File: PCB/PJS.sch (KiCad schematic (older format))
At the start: 40 parts, among them J1 HFW8R-1STE1H1LF_FFC, J10 SM02B-PASS-TBT_SwitchConnector, J2 SM02B-PASS-TBT_Connector, J3 SM02B-PASS-TBT_Connector, J4 SM02B-PASS-TBT_Connector, J5 SM02B-PASS-TBT_Connector, J6 SM02B-PASS-TBT_SwitchConnector, J7 SM02B-PASS-TBT_SwitchConnector, J8 SM02B-PASS-TBT_SwitchConnector, J9 SM02B-PASS-TBT_SwitchConnector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

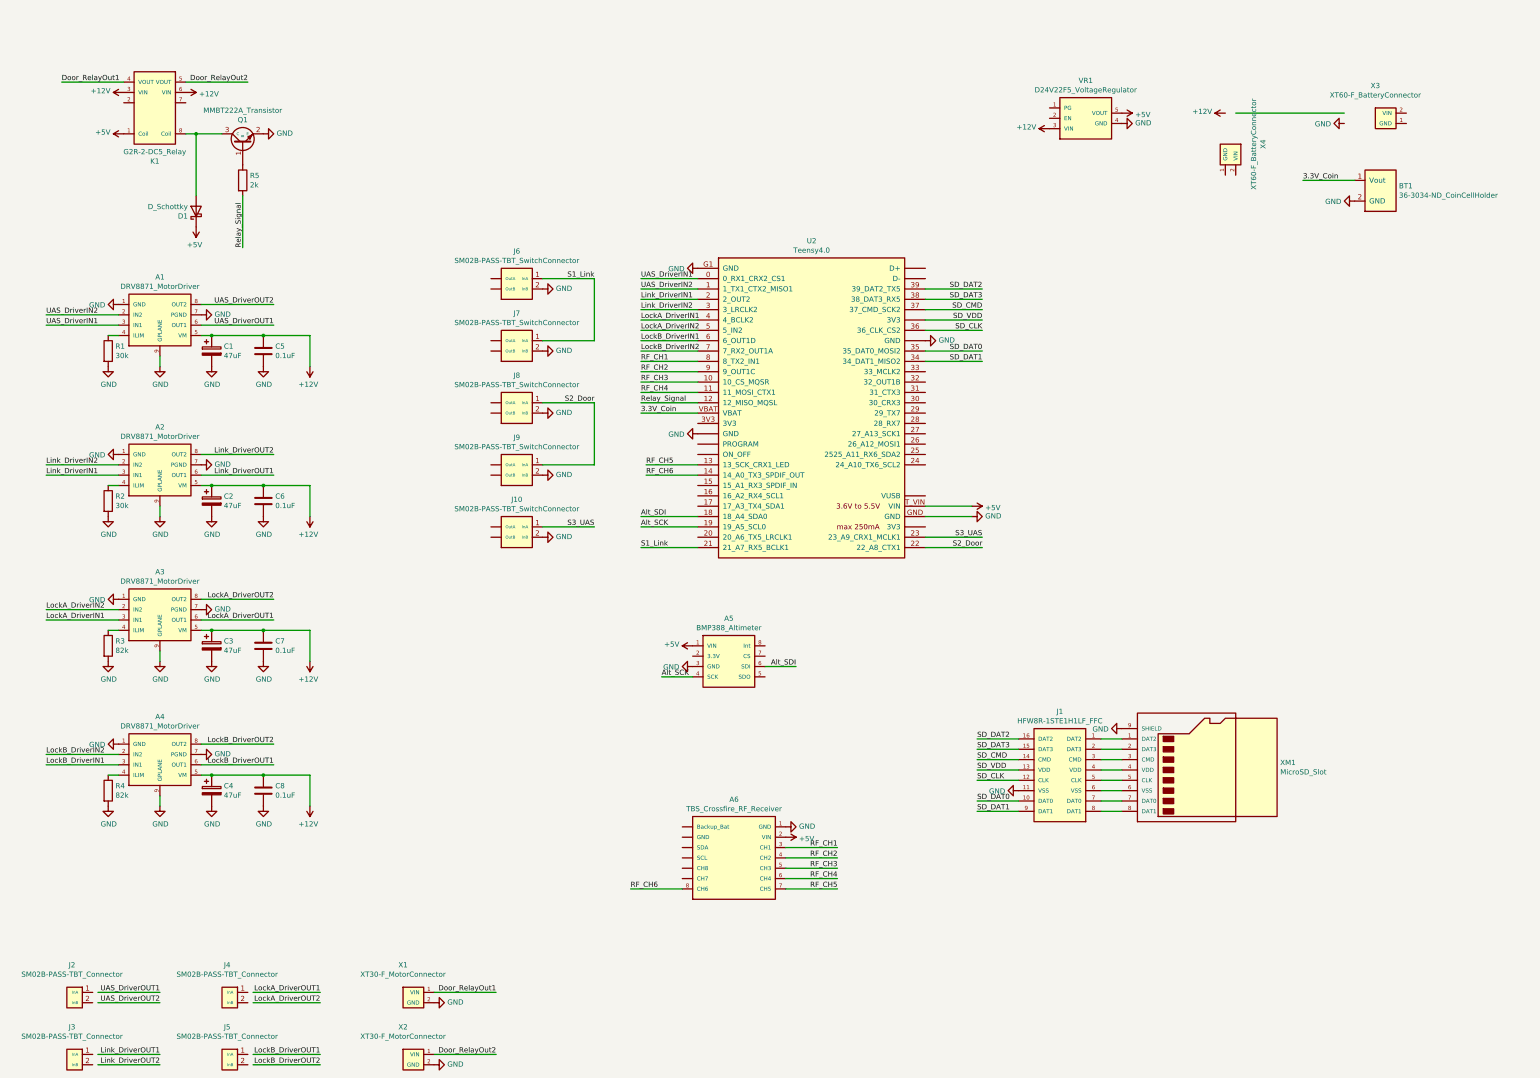
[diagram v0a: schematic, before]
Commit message: Updated connector symbols
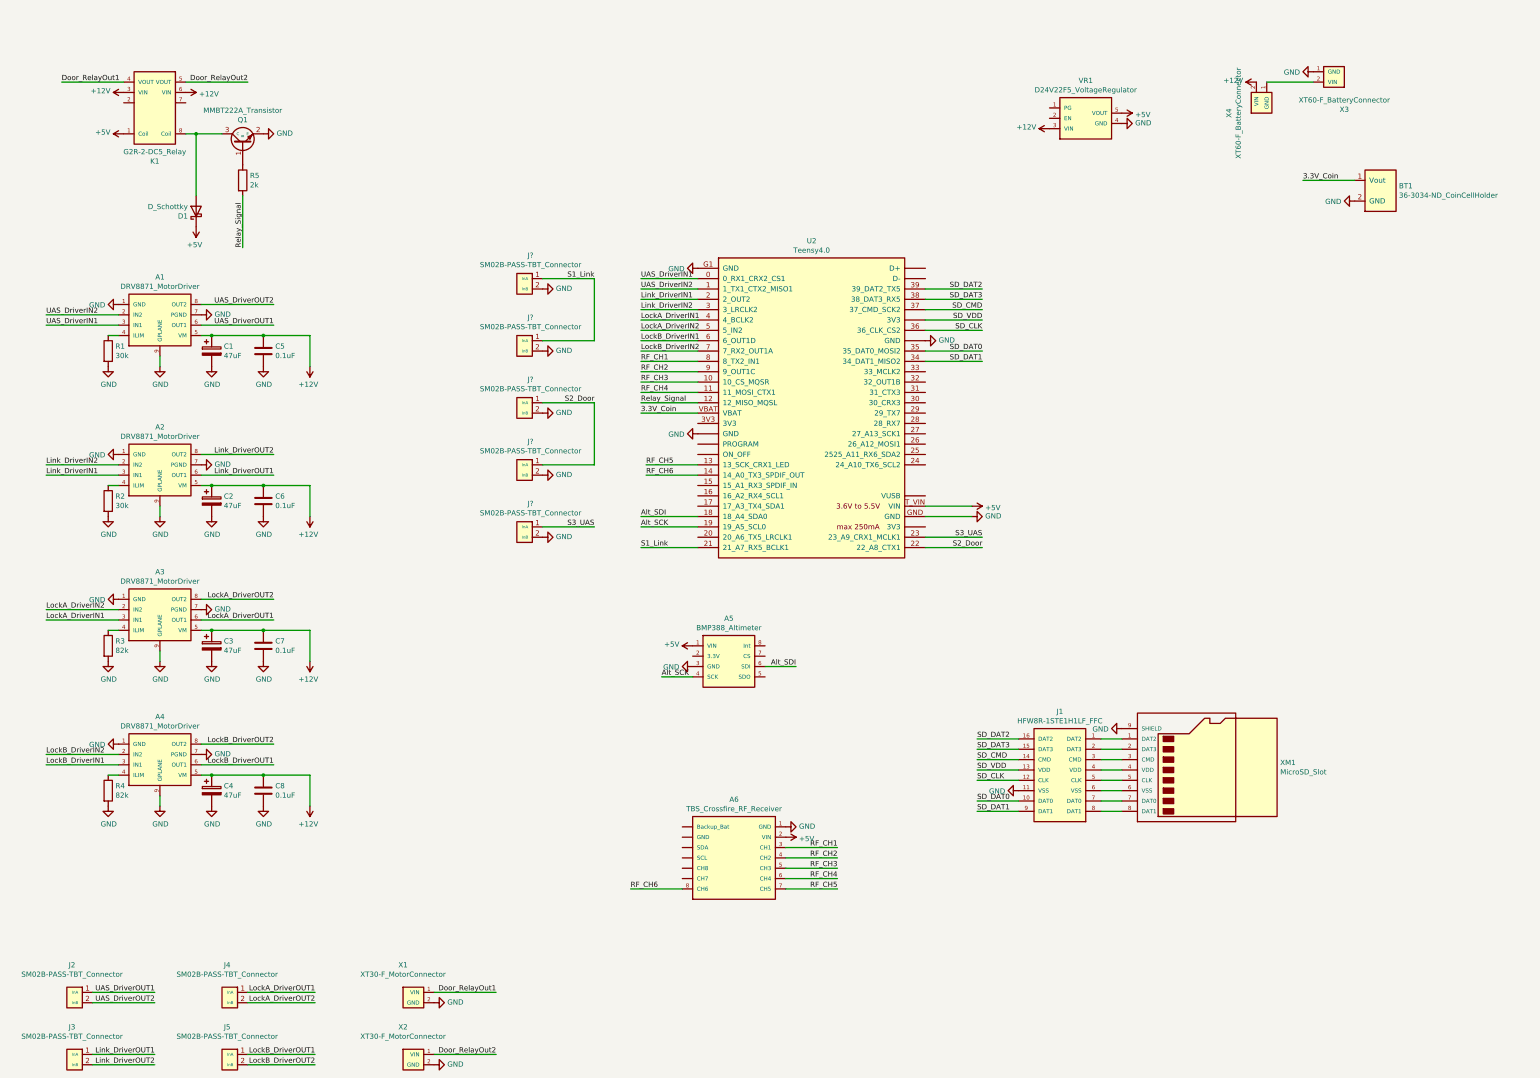
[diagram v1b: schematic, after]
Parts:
- removed J10, J6, J7, J8, J9: SM02B-PASS-TBT_SwitchConnector, PJS:SM02B-PASS-TBT_Connector, symbol PJS:SM02B-PASS-TBT_SwitchConnector
- added J? (x5): SM02B-PASS-TBT_Connector, symbol PJS:SM02B-PASS-TBT_Connector
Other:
- moved on the sheet: X3, X4
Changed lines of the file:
@@
 Wire Wire Line
 	8300 8850 8800 8850
-Text Label 2250 10150 2    50   ~ 0
+Text Label 2200 10150 2    50   ~ 0
 UAS_DriverOUT1
-Text Label 2250 10250 2    50   ~ 0
+Text Label 2200 10250 2    50   ~ 0
 UAS_DriverOUT2
 Text Label 6900 3250 0    50   ~ 0
@@
 Text Label 6900 3350 0    50   ~ 0
 UAS_DriverIN2
-Text Label 2250 10750 2    50   ~ 0
+Text Label 2200 10750 2    50   ~ 0
 Link_DriverOUT1
-Text Label 2250 10850 2    50   ~ 0
+Text Label 2200 10850 2    50   ~ 0
 Link_DriverOUT2
 $Comp
@@
 $EndComp
 Wire Wire Line
-	1650 10150 2250 10150
-Wire Wire Line
-	1650 10250 2250 10250
-Wire Wire Line
-	1650 10750 2250 10750
-Wire Wire Line
-	1650 10850 2250 10850
+	1600 10150 2200 10150
+Wire Wire Line
+	1600 10250 2200 10250
+Wire Wire Line
+	1600 10750 2200 10750
+Wire Wire Line
+	1600 10850 2200 10850
 Wire Wire Line
 	6900 5650 7450 5650
@@
 	0    -1   -1   0
 $EndComp
-Text Label 3800 10150 2    50   ~ 0
+Text Label 3750 10150 2    50   ~ 0
 LockA_DriverOUT1
-Text Label 3800 10250 2    50   ~ 0
+Text Label 3750 10250 2    50   ~ 0
 LockA_DriverOUT2
-Text Label 3800 10750 2    50   ~ 0
+Text Label 3750 10750 2    50   ~ 0
 LockB_DriverOUT1
-Text Label 3800 10850 2    50   ~ 0
+Text Label 3750 10850 2    50   ~ 0
 LockB_DriverOUT2
 Text Label 6450 4450 2    50   ~ 0
@@
 L power:GND #PWR0134
 U 1 1 5FF2647A
-P 13700 1750
-F 0 "#PWR0134" H 13700 1500 50  0001 C CNN
-F 1 "GND" V 13705 1622 50  0000 R CNN
-F 2 "" H 13700 1750 50  0001 C CNN
-F 3 "" H 13700 1750 50  0001 C CNN
-	1    13700 1750
+P 13400 1250
+F 0 "#PWR0134" H 13400 1000 50  0001 C CNN
+F 1 "GND" V 13405 1122 50  0000 R CNN
+F 2 "" H 13400 1250 50  0001 C CNN
+F 3 "" H 13400 1250 50  0001 C CNN
+	1    13400 1250
 	0    1    1    0
 $EndComp
@@
 L PJS:XT60-F_BatteryConnector X3
 U 1 1 5FF22EAF
-P 14000 1700
-F 0 "X3" H 14000 2015 50  0000 C CNN
-F 1 "XT60-F_BatteryConnector" H 14000 1924 50  0000 C CNN
-F 2 "PJS:XT60_FemaleBatteryConnector" H 14000 2200 50  0001 C CNN
-F 3 "" H 14000 2200 50  0001 C CNN
-	1    14000 1700
-	1    0    0    -1
+P 13700 1300
+F 0 "X3" H 13700 1615 50  0000 C CNN
+F 1 "XT60-F_BatteryConnector" H 13700 1524 50  0000 C CNN
+F 2 "PJS:XT60_FemaleBatteryConnector" H 13700 1800 50  0001 C CNN
+F 3 "" H 13700 1800 50  0001 C CNN
+	1    13700 1300
+	-1   0    0    1
 $EndComp
 $Comp
@@
 	2650 6650 2750 6650
 Wire Wire Line
-	3150 10850 3800 10850
-Wire Wire Line
-	3150 10750 3800 10750
-Wire Wire Line
-	3150 10250 3800 10250
-Wire Wire Line
-	3150 10150 3800 10150
+	3100 10850 3750 10850
+Wire Wire Line
+	3100 10750 3750 10750
+Wire Wire Line
+	3100 10250 3750 10250
+Wire Wire Line
+	3100 10150 3750 10150
 $Comp
 L power:GND #PWR0153
@@
 L PJS:XT60-F_BatteryConnector X4
 U 1 1 5FF20F6C
-P 12600 1950
-F 0 "X4" H 12600 2265 50  0000 C CNN
-F 1 "XT60-F_BatteryConnector" H 12600 2174 50  0000 C CNN
-F 2 "PJS:XT60_FemaleBatteryConnector" H 12600 2450 50  0001 C CNN
-F 3 "" H 12600 2450 50  0001 C CNN
-	1    12600 1950
-	0    1    1    0
-$EndComp
-Wire Wire Line
-	13700 1650 12650 1650
+P 12900 1650
+F 0 "X4" H 12900 1965 50  0000 C CNN
+F 1 "XT60-F_BatteryConnector" H 12900 1874 50  0000 C CNN
+F 2 "PJS:XT60_FemaleBatteryConnector" H 12900 2150 50  0001 C CNN
+F 3 "" H 12900 2150 50  0001 C CNN
+	1    12900 1650
+	0    -1   -1   0
+$EndComp
 $Comp
 L power:+12V #PWR0135
 U 1 1 5FF3DFBC
-P 12550 1650
-F 0 "#PWR0135" H 12550 1500 50  0001 C CNN
-F 1 "+12V" V 12565 1778 50  0000 L CNN
-F 2 "" H 12550 1650 50  0001 C CNN
-F 3 "" H 12550 1650 50  0001 C CNN
-	1    12550 1650
-	0    -1   -1   0
-$EndComp
-$Comp
-L PJS:SM02B-PASS-TBT_SwitchConnector J7
-U 1 1 5FF5A567
-P 5700 3900
-F 0 "J7" H 5700 4215 50  0000 C CNN
-F 1 "SM02B-PASS-TBT_SwitchConnector" H 5700 4124 50  0000 C CNN
-F 2 "PJS:SM02B-PASS-TBT_Connector" H 5700 4700 50  0001 C CNN
-F 3 "" H 5700 4700 50  0001 C CNN
-	1    5700 3900
-	1    0    0    -1
-$EndComp
-$Comp
-L PJS:SM02B-PASS-TBT_SwitchConnector J8
-U 1 1 5FF60366
-P 5700 4500
-F 0 "J8" H 5700 4815 50  0000 C CNN
-F 1 "SM02B-PASS-TBT_SwitchConnector" H 5700 4724 50  0000 C CNN
-F 2 "PJS:SM02B-PASS-TBT_Connector" H 5700 5300 50  0001 C CNN
-F 3 "" H 5700 5300 50  0001 C CNN
-	1    5700 4500
-	1    0    0    -1
+P 12850 1350
+F 0 "#PWR0135" H 12850 1200 50  0001 C CNN
+F 1 "+12V" V 12865 1478 50  0000 L CNN
+F 2 "" H 12850 1350 50  0001 C CNN
+F 3 "" H 12850 1350 50  0001 C CNN
+	1    12850 1350
+	0    -1   -1   0
 $EndComp
 $Comp
@@
 Text Label 6450 5650 2    50   ~ 0
 S3_UAS
-$Comp
-L PJS:SM02B-PASS-TBT_SwitchConnector J6
-U 1 1 5FF52CF4
-P 5700 3300
-F 0 "J6" H 5700 3615 50  0000 C CNN
-F 1 "SM02B-PASS-TBT_SwitchConnector" H 5700 3524 50  0000 C CNN
-F 2 "PJS:SM02B-PASS-TBT_Connector" H 5700 4100 50  0001 C CNN
-F 3 "" H 5700 4100 50  0001 C CNN
-	1    5700 3300
-	1    0    0    -1
-$EndComp
-$Comp
-L PJS:SM02B-PASS-TBT_SwitchConnector J9
-U 1 1 5FF66278
-P 5700 5100
-F 0 "J9" H 5700 5415 50  0000 C CNN
-F 1 "SM02B-PASS-TBT_SwitchConnector" H 5700 5324 50  0000 C CNN
-F 2 "PJS:SM02B-PASS-TBT_Connector" H 5700 5900 50  0001 C CNN
-F 3 "" H 5700 5900 50  0001 C CNN
-	1    5700 5100
-	1    0    0    -1
-$EndComp
-$Comp
-L PJS:SM02B-PASS-TBT_SwitchConnector J10
-U 1 1 5FF6C1E4
-P 5700 5700
-F 0 "J10" H 5700 6015 50  0000 C CNN
-F 1 "SM02B-PASS-TBT_SwitchConnector" H 5700 5924 50  0000 C CNN
-F 2 "PJS:SM02B-PASS-TBT_Connector" H 5700 6500 50  0001 C CNN
-F 3 "" H 5700 6500 50  0001 C CNN
-	1    5700 5700
-	1    0    0    -1
-$EndComp
 Wire Wire Line
 	5950 5650 6450 5650
@@
 	0    1    1    0
 $EndComp
+$Comp
+L PJS:SM02B-PASS-TBT_Connector J?
+U 1 1 5FF34C1C
+P 5750 3300
+F 0 "J?" H 5833 3575 50  0000 C CNN
+F 1 "SM02B-PASS-TBT_Connector" H 5833 3484 50  0000 C CNN
+F 2 "" H 5750 4100 50  0001 C CNN
+F 3 "" H 5750 4100 50  0001 C CNN
+	1    5750 3300
+	1    0    0    -1
+$EndComp
+$Comp
+L PJS:SM02B-PASS-TBT_Connector J?
+U 1 1 5FF35CEB
+P 5750 3900
+F 0 "J?" H 5833 4175 50  0000 C CNN
+F 1 "SM02B-PASS-TBT_Connector" H 5833 4084 50  0000 C CNN
+F 2 "" H 5750 4700 50  0001 C CNN
+F 3 "" H 5750 4700 50  0001 C CNN
+	1    5750 3900
+	1    0    0    -1
+$EndComp
+$Comp
+L PJS:SM02B-PASS-TBT_Connector J?
+U 1 1 5FF3C0BA
+P 5750 4500
+F 0 "J?" H 5833 4775 50  0000 C CNN
+F 1 "SM02B-PASS-TBT_Connector" H 5833 4684 50  0000 C CNN
+F 2 "" H 5750 5300 50  0001 C CNN
+F 3 "" H 5750 5300 50  0001 C CNN
+	1    5750 4500
+	1    0    0    -1
+$EndComp
+$Comp
+L PJS:SM02B-PASS-TBT_Connector J?
+U 1 1 5FF423A5
+P 5750 5100
+F 0 "J?" H 5833 5375 50  0000 C CNN
+F 1 "SM02B-PASS-TBT_Connector" H 5833 5284 50  0000 C CNN
+F 2 "" H 5750 5900 50  0001 C CNN
+F 3 "" H 5750 5900 50  0001 C CNN
+	1    5750 5100
+	1    0    0    -1
+$EndComp
+$Comp
+L PJS:SM02B-PASS-TBT_Connector J?
+U 1 1 5FF486F6
+P 5750 5700
+F 0 "J?" H 5833 5975 50  0000 C CNN
+F 1 "SM02B-PASS-TBT_Connector" H 5833 5884 50  0000 C CNN
+F 2 "" H 5750 6500 50  0001 C CNN
+F 3 "" H 5750 6500 50  0001 C CNN
+	1    5750 5700
+	1    0    0    -1
+$EndComp
+Wire Wire Line
+	13400 1350 12950 1350
 $EndSCHEMATC

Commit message: Nearly Finished PCB
Requires resizing footprint for the altimeter. New resistors on the motor driver ICs need to be implemented. Perhaps ground planes/heat dissapation should be added to the driver ICs.
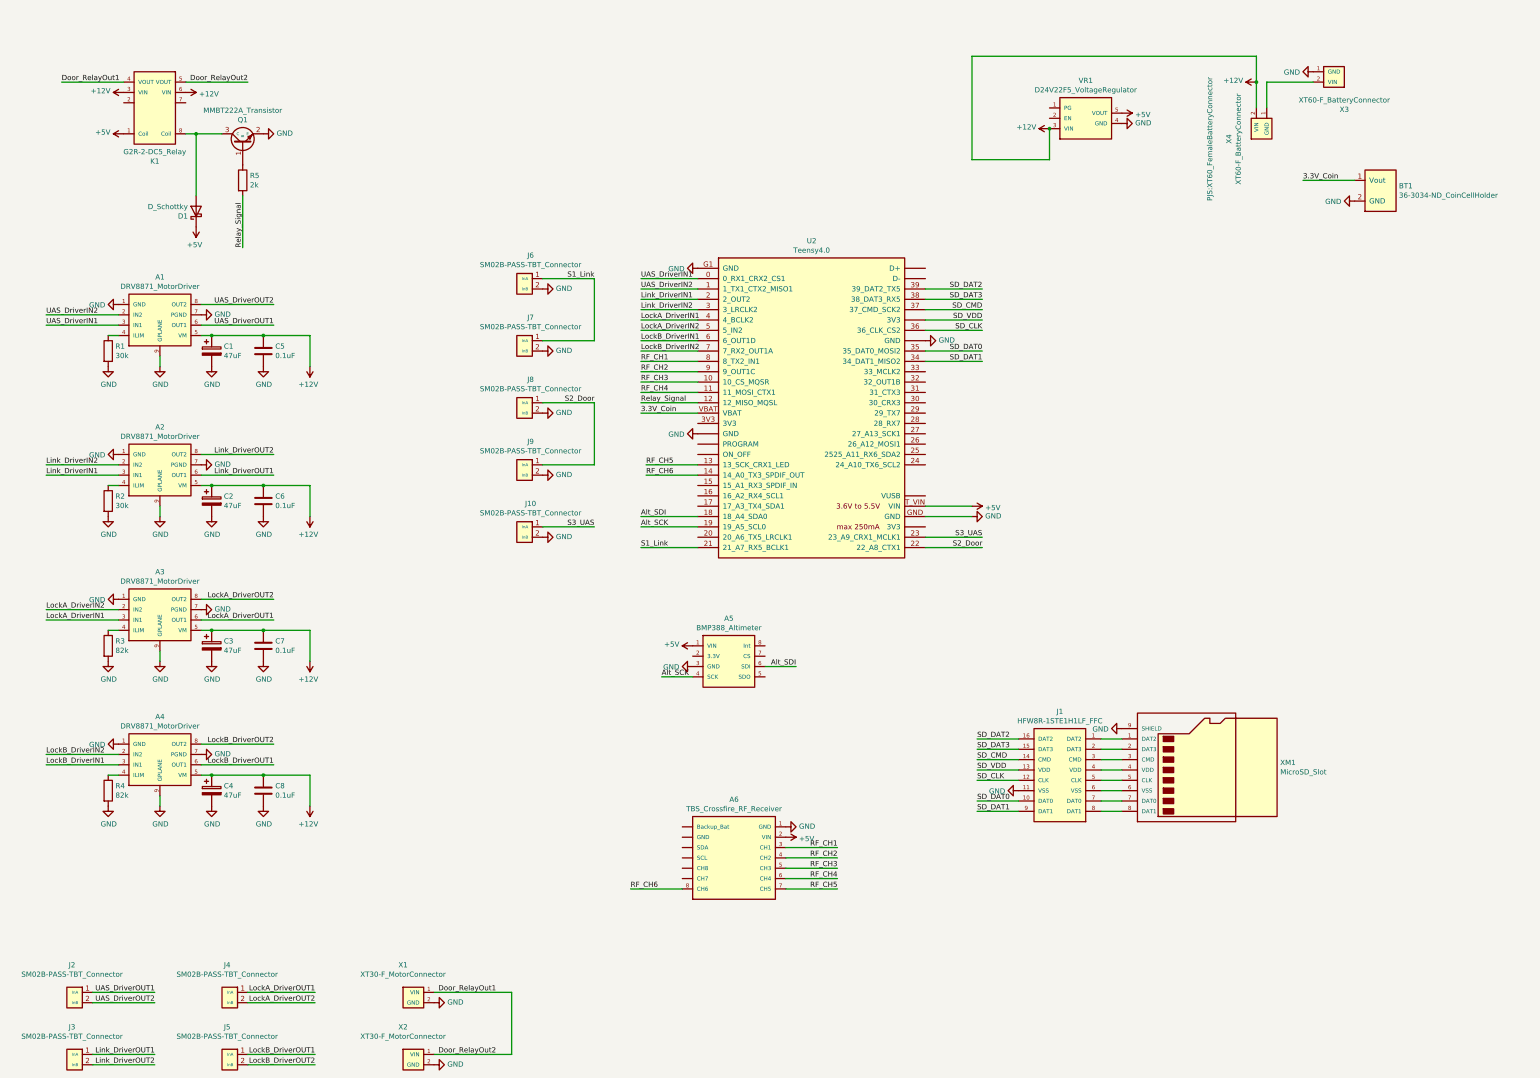
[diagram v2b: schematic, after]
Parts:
- gave numbers to parts that had none: 5
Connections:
- net Door_RelayOut2 is gone; now on net Door_RelayOut1: K1.5 (VOUT), X2.1 (VIN)
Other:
- moved on the sheet: X4
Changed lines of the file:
@@
 	0    -1   -1   0
 $EndComp
-Wire Wire Line
-	4900 10750 5500 10750
 $Comp
 L PJS:XT30-F_MotorConnector X2
@@
 	1    0    0    -1
 $EndComp
-Wire Wire Line
-	4900 10150 5500 10150
 Text Label 5500 10750 2    50   ~ 0
 Door_RelayOut2
@@
 L PJS:XT60-F_BatteryConnector X4
 U 1 1 5FF20F6C
-P 12900 1650
-F 0 "X4" H 12900 1965 50  0000 C CNN
-F 1 "XT60-F_BatteryConnector" H 12900 1874 50  0000 C CNN
-F 2 "PJS:XT60_FemaleBatteryConnector" H 12900 2150 50  0001 C CNN
-F 3 "" H 12900 2150 50  0001 C CNN
-	1    12900 1650
+P 12900 1900
+F 0 "X4" H 12900 2215 50  0000 C CNN
+F 1 "XT60-F_BatteryConnector" H 12900 2124 50  0000 C CNN
+F 2 "PJS:XT60_FemaleBatteryConnector" H 12900 2400 50  0000 C CNN
+F 3 "" H 12900 2400 50  0001 C CNN
+	1    12900 1900
 	0    -1   -1   0
 $EndComp
@@
 $EndComp
 $Comp
-L PJS:SM02B-PASS-TBT_Connector J?
+L PJS:SM02B-PASS-TBT_Connector J6
 U 1 1 5FF34C1C
 P 5750 3300
-F 0 "J?" H 5833 3575 50  0000 C CNN
+F 0 "J6" H 5833 3575 50  0000 C CNN
 F 1 "SM02B-PASS-TBT_Connector" H 5833 3484 50  0000 C CNN
 F 2 "" H 5750 4100 50  0001 C CNN
@@
 $EndComp
 $Comp
-L PJS:SM02B-PASS-TBT_Connector J?
+L PJS:SM02B-PASS-TBT_Connector J7
 U 1 1 5FF35CEB
 P 5750 3900
-F 0 "J?" H 5833 4175 50  0000 C CNN
+F 0 "J7" H 5833 4175 50  0000 C CNN
 F 1 "SM02B-PASS-TBT_Connector" H 5833 4084 50  0000 C CNN
 F 2 "" H 5750 4700 50  0001 C CNN
@@
 $EndComp
 $Comp
-L PJS:SM02B-PASS-TBT_Connector J?
+L PJS:SM02B-PASS-TBT_Connector J8
 U 1 1 5FF3C0BA
 P 5750 4500
-F 0 "J?" H 5833 4775 50  0000 C CNN
+F 0 "J8" H 5833 4775 50  0000 C CNN
 F 1 "SM02B-PASS-TBT_Connector" H 5833 4684 50  0000 C CNN
 F 2 "" H 5750 5300 50  0001 C CNN
@@
 $EndComp
 $Comp
-L PJS:SM02B-PASS-TBT_Connector J?
+L PJS:SM02B-PASS-TBT_Connector J9
 U 1 1 5FF423A5
 P 5750 5100
-F 0 "J?" H 5833 5375 50  0000 C CNN
+F 0 "J9" H 5833 5375 50  0000 C CNN
 F 1 "SM02B-PASS-TBT_Connector" H 5833 5284 50  0000 C CNN
 F 2 "" H 5750 5900 50  0001 C CNN
@@
 $EndComp
 $Comp
-L PJS:SM02B-PASS-TBT_Connector J?
+L PJS:SM02B-PASS-TBT_Connector J10
 U 1 1 5FF486F6
 P 5750 5700
-F 0 "J?" H 5833 5975 50  0000 C CNN
+F 0 "J10" H 5833 5975 50  0000 C CNN
 F 1 "SM02B-PASS-TBT_Connector" H 5833 5884 50  0000 C CNN
 F 2 "" H 5750 6500 50  0001 C CNN
@@
 Wire Wire Line
 	13400 1350 12950 1350
+Wire Wire Line
+	5650 10150 5650 10750
+Wire Wire Line
+	4900 10750 5650 10750
+Wire Wire Line
+	4900 10150 5650 10150
+Wire Wire Line
+	12950 1600 12950 1350
+Wire Wire Line
+	12850 1600 12850 1350
+Wire Wire Line
+	12850 1350 12850 1100
+Wire Wire Line
+	12850 1100 10100 1100
+Wire Wire Line
+	10100 1100 10100 2100
+Wire Wire Line
+	10100 2100 10850 2100
+Wire Wire Line
+	10850 2100 10850 1800
+Connection ~ 12850 1350
+Connection ~ 10850 1800
 $EndSCHEMATC

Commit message: Silkscreen Memes and Clear Relay CAD
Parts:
- R5: footprint PJS:RMCF2512FT2K00_Resistor -> PJS:ERA-6AEB202V
- X1, X2: footprint PJS:XT30_Female_MotorConnector -> Connector_AMASS:AMASS_XT30U-F_1x02_P5.0mm_Vertical
- X3, X4: footprint PJS:XT60_FemaleBatteryConnector -> Connector_AMASS:AMASS_XT60-M_1x02_P7.20mm_Vertical
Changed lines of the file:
@@
 F 0 "X3" H 13700 1615 50  0000 C CNN
 F 1 "XT60-F_BatteryConnector" H 13700 1524 50  0000 C CNN
-F 2 "PJS:XT60_FemaleBatteryConnector" H 13700 1800 50  0001 C CNN
+F 2 "Connector_AMASS:AMASS_XT60-M_1x02_P7.20mm_Vertical" H 13700 1800 50  0001 C CNN
 F 3 "" H 13700 1800 50  0001 C CNN
 	1    13700 1300
@@
 F 0 "X2" H 4600 11115 50  0000 C CNN
 F 1 "XT30-F_MotorConnector" H 4600 11024 50  0000 C CNN
-F 2 "PJS:XT30_Female_MotorConnector" H 4600 11000 50  0001 C CNN
+F 2 "Connector_AMASS:AMASS_XT30U-F_1x02_P5.0mm_Vertical" H 4600 11000 50  0001 C CNN
 F 3 "" H 4600 11000 50  0001 C CNN
 	1    4600 10800
@@
 F 0 "X1" H 4600 10515 50  0000 C CNN
 F 1 "XT30-F_MotorConnector" H 4600 10424 50  0000 C CNN
-F 2 "PJS:XT30_Female_MotorConnector" H 4600 10400 50  0001 C CNN
+F 2 "Connector_AMASS:AMASS_XT30U-F_1x02_P5.0mm_Vertical" H 4600 10400 50  0001 C CNN
 F 3 "" H 4600 10400 50  0001 C CNN
 	1    4600 10200
@@
 F 0 "X4" H 12900 2215 50  0000 C CNN
 F 1 "XT60-F_BatteryConnector" H 12900 2124 50  0000 C CNN
-F 2 "PJS:XT60_FemaleBatteryConnector" H 12900 2400 50  0000 C CNN
+F 2 "Connector_AMASS:AMASS_XT60-M_1x02_P7.20mm_Vertical" H 12900 2400 50  0000 C CNN
 F 3 "" H 12900 2400 50  0001 C CNN
 	1    12900 1900
@@
 F 0 "R5" H 3120 2346 50  0000 L CNN
 F 1 "2k" H 3120 2255 50  0000 L CNN
-F 2 "PJS:RMCF2512FT2K00_Resistor" V 2980 2300 50  0001 C CNN
+F 2 "PJS:ERA-6AEB202V" V 2980 2300 50  0001 C CNN
 F 3 "~" H 3050 2300 50  0001 C CNN
 	1    3050 2300
